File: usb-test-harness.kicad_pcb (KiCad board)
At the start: 4 copper layers, 98 x 85 mm, 85 parts, among them J1 5V_RAW, J10 USB_A_DUAL, J2 GND, J3 V_EXT, J4 USB_A (female down), J5 Conn_01x03_Male, J6 USB_A_DUAL, J7 USB_A_DUAL, J8 USB_A SOFNG USB-05, J9 USB_B_Micro (up), U1 FT24C02A, U2 SE5120ST33, U3 USB2517, U4 APL3511C, U5 APL3511C, U6 APL3511C, U7 APL3511C, U8 APL3511C, U9 APL3511C, Y1 24MHz

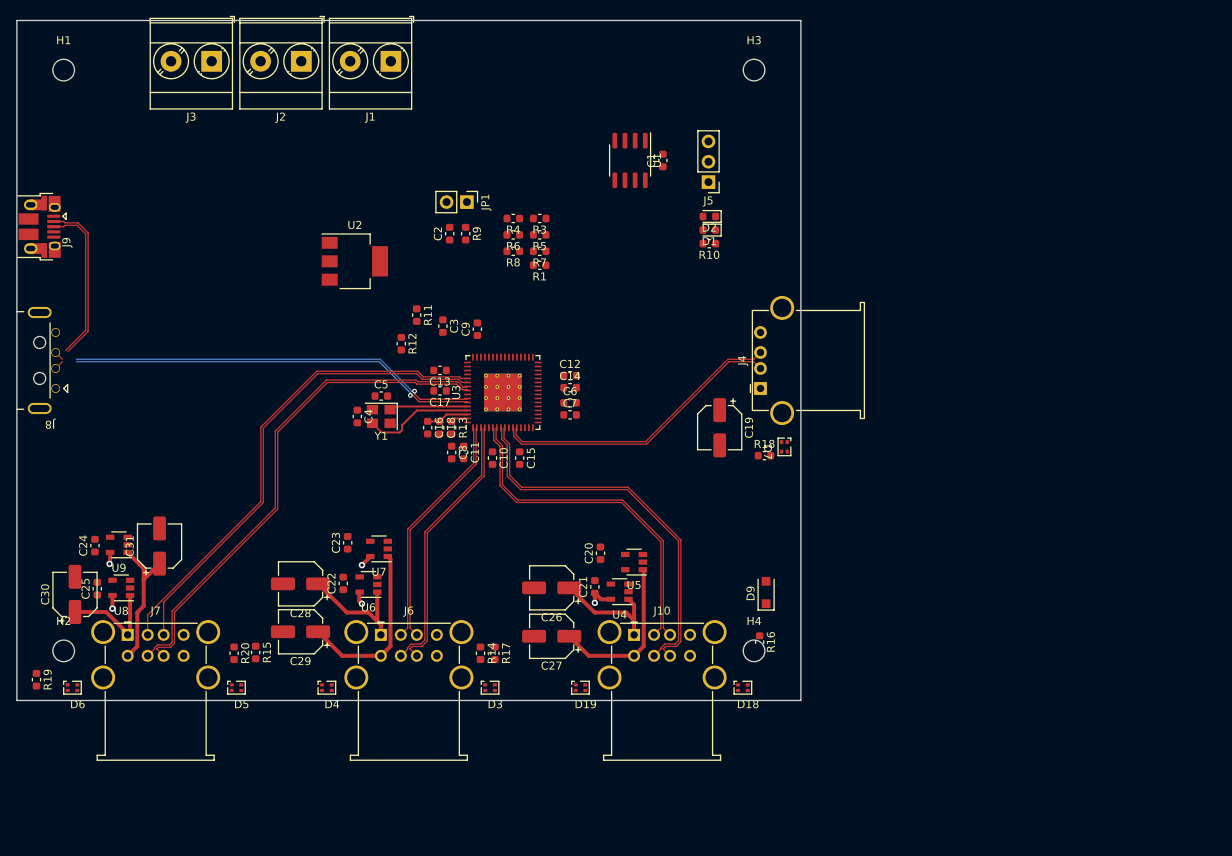
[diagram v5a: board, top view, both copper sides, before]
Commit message: usb-hub: switch to newer amphenol micro b
this makes it feasible to route usb properly.  Then, charge ahead with
routing.  Started with the 3v3 and hub power parts, now continuing with
the enable/overcurrent parts.  leds will be last.
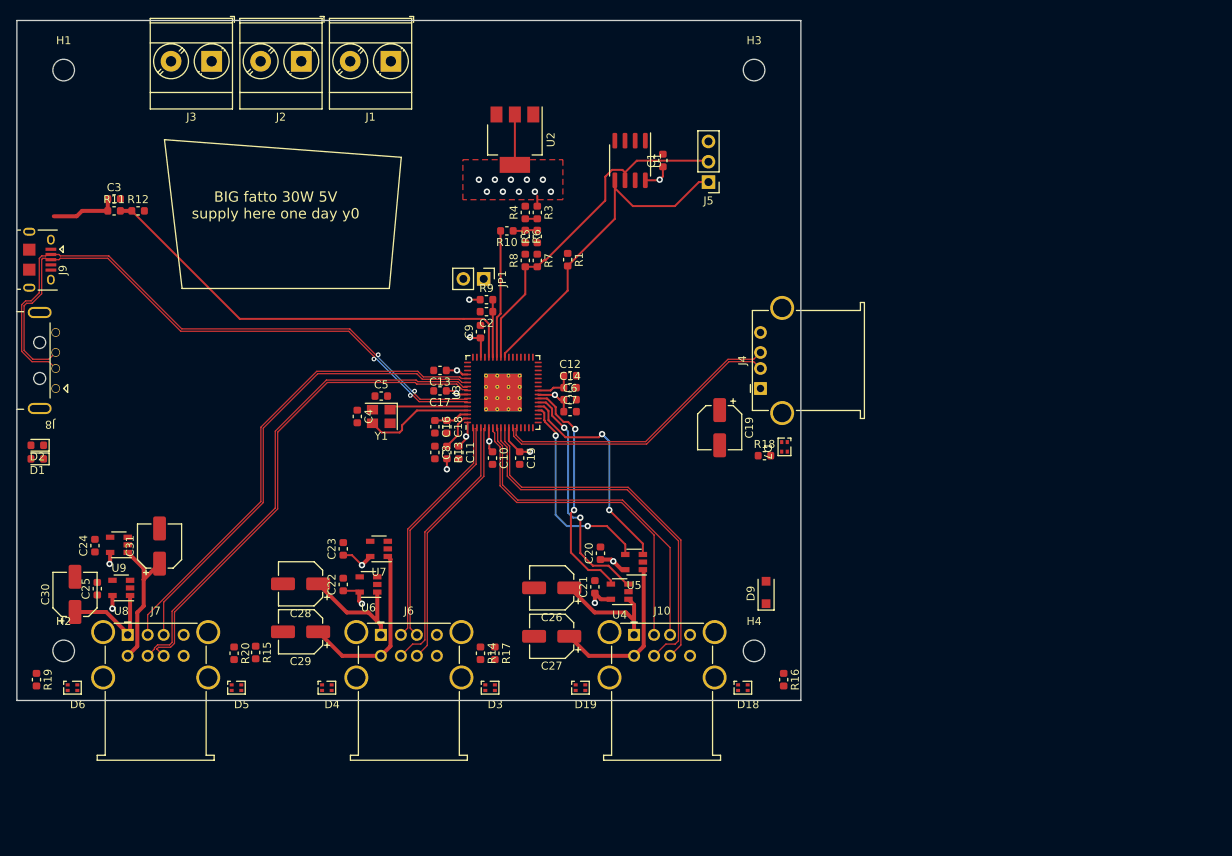
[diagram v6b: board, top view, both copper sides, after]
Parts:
- J9: footprint Connector_USB:USB_Micro-B_Amphenol_10103594-0001LF_Horizontal -> Connector_USB:USB_Micro-B_Amphenol_10118194-0001LF_Horizontal
- moved D1 88.7 mm to (101.8, 105.4)
- moved D2 88.7 mm to (101.8, 103.7)
- moved C3 44.1 mm to (111.4, 72.9), turned to 0 degrees
- moved R11 40.0 mm to (111.4, 74.4), turned to 0 degrees
- moved R12 36.9 mm to (114.4, 74.4), turned to 0 degrees
- moved R10 25.4 mm to (160.5, 76.9)
- moved U2 25.1 mm to (161.5, 65.5), turned to -90 degrees
- moved C2 10.8 mm to (157.9, 87.0), turned to 180 degrees
- moved JP1 9.83 mm to (157.6, 82.9)
- moved R9 8.65 mm to (157.9, 85.5), turned to 0 degrees
- moved R16 5.58 mm to (195.1, 133.0)
- moved J9 4.30 mm to (100.8, 80.5)
- moved R1 3.57 mm to (168.1, 80.5), turned to -90 degrees
- moved R13 3.16 mm to (153.0, 104.6)
- moved C8 2.10 mm to (151.5, 104.6)
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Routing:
- net /upstream-config-leds/VBUS_DET: track 0.00 -> 56.1 mm
- net /upstream-config-leds/CFG_SEL0: track 0.00 -> 44.0 mm
- net /upstream-config-leds/EE_SDA: track 0.00 -> 42.7 mm
- net +3V3: track 0.00 -> 38.5 mm, vias 0 -> 19
- net /downstream-port-power/OC1: track 0.00 -> 29.7 mm, vias 0 -> 2
- net /downstream-port-power/EN1: track 0.00 -> 29.3 mm, vias 0 -> 2
- net /downstream-port-power/OC2: track 0.00 -> 27.6 mm, vias 0 -> 2
- net /downstream-port-power/EN2: track 0.00 -> 25.8 mm, vias 0 -> 2
- net /upstream-config-leds/CFG_SEL1_A: track 0.00 -> 16.0 mm
- net +5V: track 9.62 -> 18.2 mm, vias 5 -> 6
- net /upstream-config-leds/VBUS_UP: track 0.00 -> 8.53 mm
- net /upstream-config-leds/~RESET: track 0.00 -> 7.19 mm
- net /upstream-config-leds/UP-: track 73.1 -> 79.7 mm, vias 1 -> 2
- net /upstream-config-leds/UP+: track 72.5 -> 78.7 mm, vias 1 -> 2
- net /upstream-config-leds/VDD18: track 0.00 -> 4.84 mm
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- added copper zone on F.Cu, net +3V3
- added copper zone on In2.Cu, net +3V3
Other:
- board text added: "BIG fatto 30W 5V supply here one day y0"

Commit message: usb-hub: finish all enable/oc lines, fix warnings
just leds, led drive, usb shields, and the big 5v mainline left.
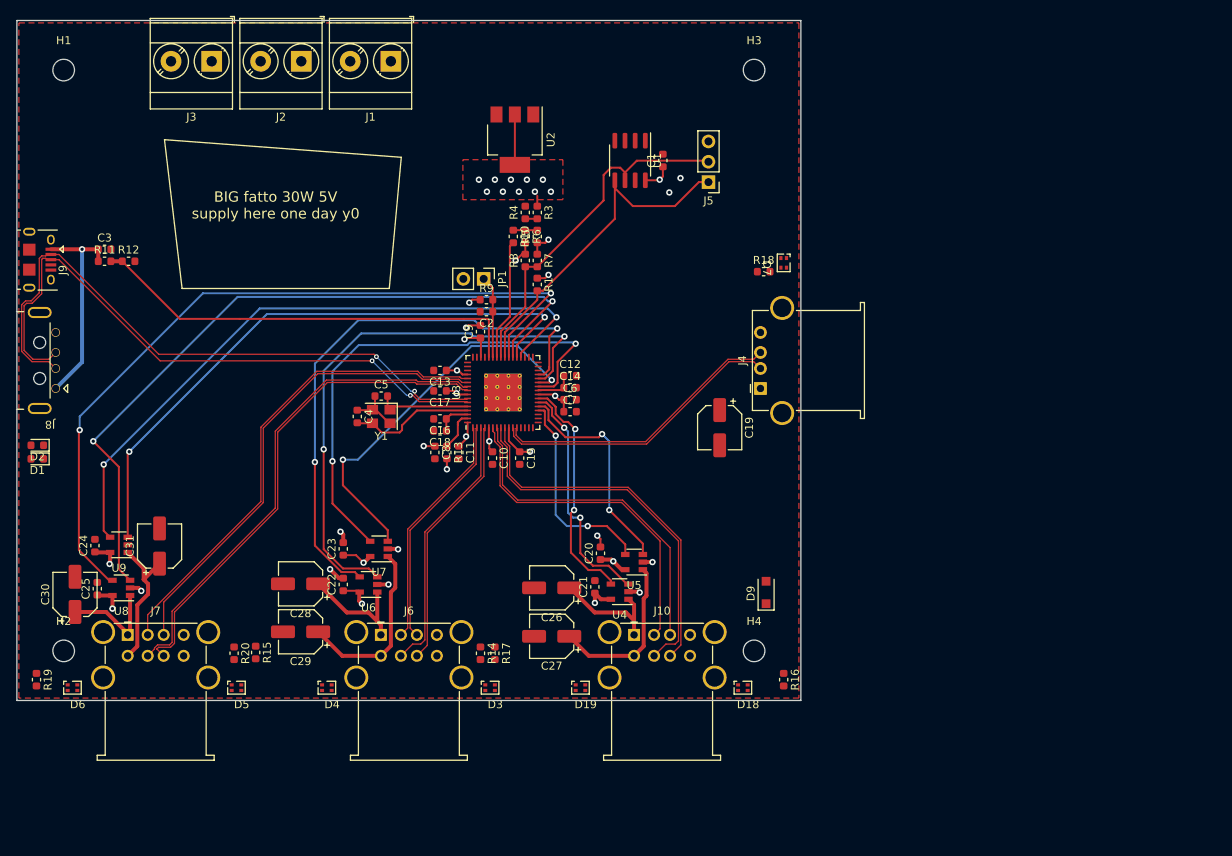
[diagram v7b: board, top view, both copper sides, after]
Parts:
- moved D7 23.0 mm to (195.1, 80.9)
- moved R18 23.0 mm to (192.6, 82.0)
- moved C3 6.41 mm to (110.2, 79.2)
- moved R11 6.41 mm to (110.2, 80.7)
- moved R12 6.41 mm to (113.2, 80.7)
- moved R1 4.90 mm to (164.3, 83.6)
- moved C16 1.18 mm to (152.1, 100.4), turned to 180 degrees
- moved R10 1.06 mm to (161.3, 77.6), turned to -90 degrees
- moved C18 1.00 mm to (152.1, 101.9), turned to 180 degrees
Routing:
- net /downstream-port-power/EN5: track 0.00 -> 97.9 mm, vias 0 -> 2
- net /downstream-port-power/OC5: track 0.00 -> 93.4 mm, vias 0 -> 2
- net /downstream-port-power/EN6: track 0.00 -> 81.4 mm, vias 0 -> 2
- net /downstream-port-power/OC6: track 0.00 -> 76.4 mm, vias 0 -> 2
- net /downstream-port-power/EN3: track 0.00 -> 70.1 mm, vias 0 -> 2
- net /downstream-port-power/OC3: track 0.00 -> 69.7 mm, vias 0 -> 2
- net /downstream-port-power/EN4: track 0.00 -> 63.6 mm, vias 0 -> 2
- net /downstream-port-power/OC4: track 0.00 -> 48.1 mm, vias 0 -> 2
- net GND: track 1.31 -> 24.9 mm, vias 1 -> 13
- net /upstream-config-leds/VBUS_UP: track 8.53 -> 26.2 mm, vias 0 -> 1
- net +3V3: track 38.5 -> 45.3 mm, vias 19 -> 22
- net +5V: track 18.2 -> 21.8 mm
- net /upstream-config-leds/~RESET: track 7.19 -> 10.3 mm
- net /upstream-config-leds/XTAL1: track 13.9 -> 15.8 mm
- net /upstream-config-leds/XTAL2: track 9.85 -> 11.7 mm
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- added copper zone on F.Cu, net GND

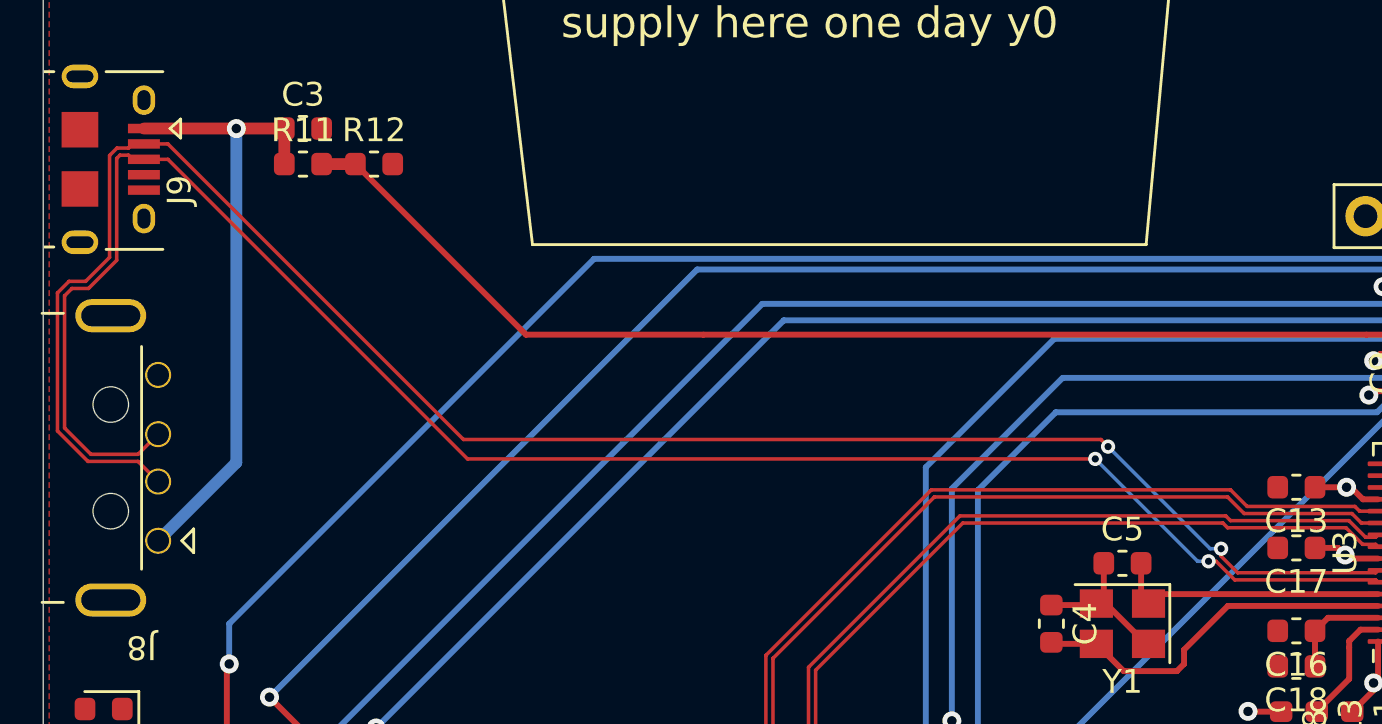
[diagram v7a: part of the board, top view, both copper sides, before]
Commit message: usb-hub: fix broken diff pair after push n shove
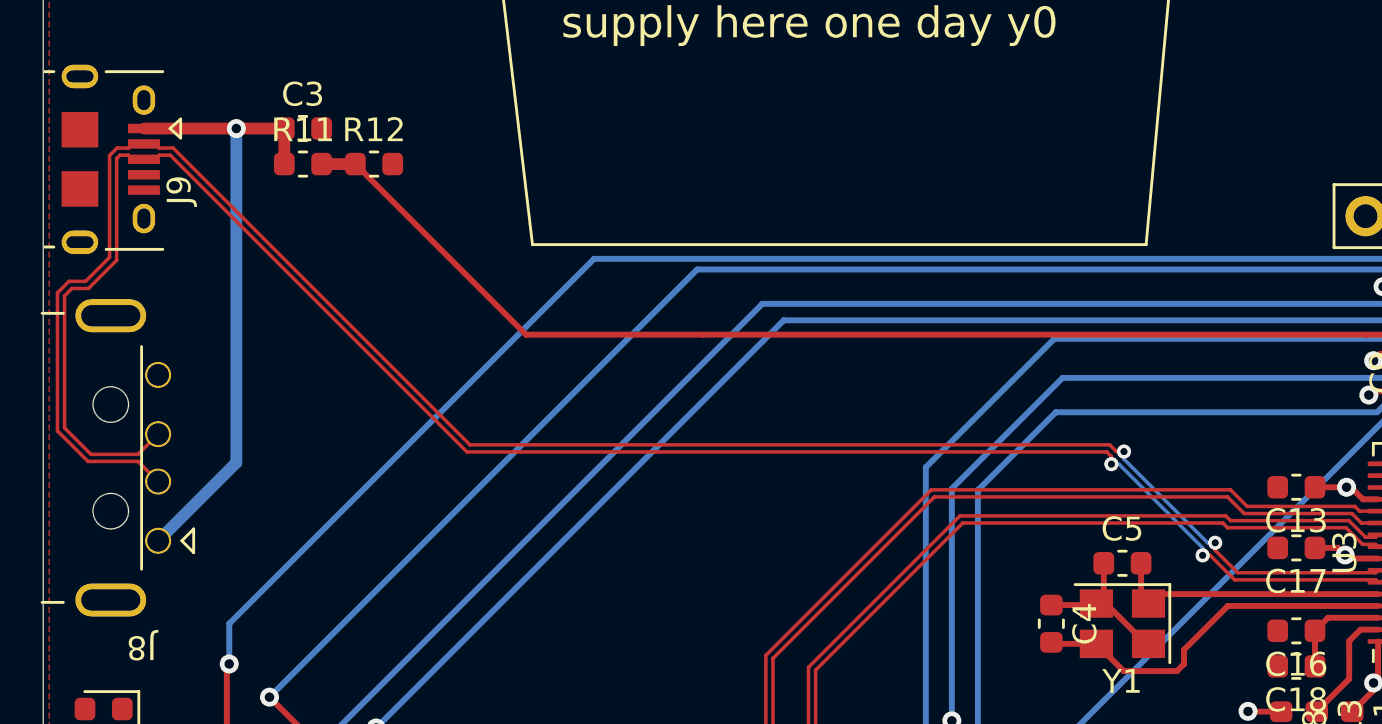
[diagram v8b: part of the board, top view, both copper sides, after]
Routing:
- net /upstream-config-leds/UP+: track 78.2 -> 78.7 mm
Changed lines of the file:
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@@
     (thickness 1.6)
     (drawings 10)
-    (tracks 567)
+    (tracks 576)
     (modules 85)
     (nets 72)
@@
   (gr_line (start 197.25 50.6) (end 99.25 50.6) (layer "Edge.Cuts") (width 0.05))
   (gr_line (start 197.25 135.6) (end 197.25 50.6) (layer "Edge.Cuts") (width 0.05))
+  (segment (start 104.15 80.325) (end 103.975 80.5) (width 0.15) (layer "F.Cu") (net 18))
+  (segment (start 104.612866 80.325) (end 104.15 80.325) (width 0.15) (layer "F.Cu") (net 18))
+  (segment (start 144.334834 93.046967) (end 144.137867 92.85) (width 0.15) (layer "F.Cu") (net 18))
+  (segment (start 117.262134 92.55) (end 104.737134 80.025) (width 0.15) (layer "F.Cu") (net 19))
+  (segment (start 144.865166 92.834834) (end 144.546967 92.834834) (width 0.15) (layer "F.Cu") (net 19))
+  (segment (start 103.975 80.5) (end 103.5 80.5) (width 0.15) (layer "F.Cu") (net 18))
+  (segment (start 117.137866 92.85) (end 104.612866 80.325) (width 0.15) (layer "F.Cu") (net 18))
+  (segment (start 144.262133 92.55) (end 117.262134 92.55) (width 0.15) (layer "F.Cu") (net 19))
+  (segment (start 144.137867 92.85) (end 117.137866 92.85) (width 0.15) (layer "F.Cu") (net 18))
+  (segment (start 144.546967 92.834834) (end 144.262133 92.55) (width 0.15) (layer "F.Cu") (net 19))
+  (segment (start 144.334834 93.365166) (end 144.334834 93.046967) (width 0.15) (layer "F.Cu") (net 18))
+  (segment (start 103.975 79.85) (end 103.5 79.85) (width 0.15) (layer "F.Cu") (net 19))
+  (segment (start 104.737134 80.025) (end 104.15 80.025) (width 0.15) (layer "F.Cu") (net 19))
+  (segment (start 104.15 80.025) (end 103.975 79.85) (width 0.15) (layer "F.Cu") (net 19))
+  (segment (start 144.653033 93.365166) (end 144.334834 93.365166) (width 0.15) (layer "B.Cu") (net 18))
+  (via (at 144.334834 93.365166) (size 0.6) (drill 0.3) (layers "F.Cu" "B.Cu") (net 18))
+  (segment (start 144.865166 93.153033) (end 144.865166 92.834834) (width 0.15) (layer "B.Cu") (net 19))
+  (segment (start 148.184834 97.215166) (end 148.184834 96.896967) (width 0.15) (layer "B.Cu") (net 18))
+  (segment (start 148.184834 96.896967) (end 144.653033 93.365166) (width 0.15) (layer "B.Cu") (net 18))
+  (via (at 144.865166 92.834834) (size 0.6) (drill 0.3) (layers "F.Cu" "B.Cu") (net 19))
+  (segment (start 148.715166 96.684834) (end 148.396967 96.684834) (width 0.15) (layer "B.Cu") (net 19))
+  (segment (start 148.396967 96.684834) (end 144.865166 93.153033) (width 0.15) (layer "B.Cu") (net 19))
+  (via (at 148.715166 96.684834) (size 0.6) (drill 0.3) (layers "F.Cu" "B.Cu") (net 19))
+  (segment (start 155.4875 97.95) (end 149.662133 97.95) (width 0.15) (layer "F.Cu") (net 19))
+  (segment (start 149.662133 97.95) (end 148.715166 97.003033) (width 0.15) (layer "F.Cu") (net 19))
+  (via (at 148.184834 97.215166) (size 0.6) (drill 0.3) (layers "F.Cu" "B.Cu") (net 18))
+  (segment (start 155.5875 98.35) (end 155.4875 98.25) (width 0.15) (layer "F.Cu") (net 18))
+  (segment (start 155.5875 97.85) (end 155.4875 97.95) (width 0.15) (layer "F.Cu") (net 19))
+  (segment (start 155.4875 98.25) (end 149.537867 98.25) (width 0.15) (layer "F.Cu") (net 18))
+  (segment (start 149.537867 98.25) (end 148.503033 97.215166) (width 0.15) (layer "F.Cu") (net 18))
+  (segment (start 148.503033 97.215166) (end 148.184834 97.215166) (width 0.15) (layer "F.Cu") (net 18))
+  (segment (start 148.715166 97.003033) (end 148.715166 96.684834) (width 0.15) (layer "F.Cu") (net 19))
   (segment (start 158.3 104.1125) (end 158.7 104.5125) (width 0.25) (layer "F.Cu") (net 6) (status 8000))
   (segment (start 158.25 103.15) (end 158.3 103.2) (width 0.25) (layer "F.Cu") (net 6) (status 8000))
@@
   (via (at 166.7 87.7) (size 0.8) (drill 0.4) (layers "F.Cu" "B.Cu") (net 26))
   (segment (start 145.6156 114.3156) (end 145.6156 115.7) (width 0.25) (layer "F.Cu") (net 36))
-  (segment (start 147.973407 97.465166) (end 143.653258 93.145017) (width 0.15) (layer "B.Cu") (net 18))
   (via (at 140 105.5) (size 0.8) (drill 0.4) (layers "F.Cu" "B.Cu") (net 36))
-  (segment (start 148.965166 96.934834) (end 148.503554 96.934834) (width 0.15) (layer "B.Cu") (net 19))
-  (segment (start 103.5 80.5) (end 104.512501 80.5) (width 0.15) (layer "F.Cu") (net 18))
-  (via (at 144.19373 92.62501) (size 0.6) (drill 0.3) (layers "F.Cu" "B.Cu") (net 19))
-  (segment (start 117.157518 93.145017) (end 143.653258 93.145017) (width 0.15) (layer "F.Cu") (net 18))
   (segment (start 138.7 110.9844) (end 138.7 105.7) (width 0.25) (layer "F.Cu") (net 37) (status 8000))
-  (via (at 143.653258 93.145017) (size 0.6) (drill 0.3) (layers "F.Cu" "B.Cu") (net 18))
   (segment (start 140 105.5) (end 140 108.7) (width 0.25) (layer "F.Cu") (net 36))
-  (segment (start 148.434834 97.465166) (end 147.973407 97.465166) (width 0.15) (layer "B.Cu") (net 18))
-  (segment (start 103.5 79.85) (end 104.512501 79.85) (width 0.15) (layer "F.Cu") (net 19))
-  (segment (start 104.512501 79.85) (end 116.987512 92.325011) (width 0.15) (layer "F.Cu") (net 19))
-  (segment (start 143.893731 92.325011) (end 144.19373 92.62501) (width 0.15) (layer "F.Cu") (net 19))
   (segment (start 143.4156 115.7) (end 138.7 110.9844) (width 0.25) (layer "F.Cu") (net 37) (status 8000))
-  (segment (start 148.503554 96.934834) (end 144.19373 92.62501) (width 0.15) (layer "B.Cu") (net 19))
-  (segment (start 104.512501 80.5) (end 117.157518 93.145017) (width 0.15) (layer "F.Cu") (net 18))
-  (segment (start 116.987512 92.325011) (end 143.893731 92.325011) (width 0.15) (layer "F.Cu") (net 19))
   (segment (start 140 108.7) (end 145.6156 114.3156) (width 0.25) (layer "F.Cu") (net 36))
   (via (at 138.7 105.7) (size 0.8) (drill 0.4) (layers "F.Cu" "B.Cu") (net 37))
@@
   (segment (start 160.75 101.5125) (end 160.75 103.1625) (width 0.25) (layer "F.Cu") (net 6))
   (segment (start 160.75 103.1625) (end 162.1 104.5125) (width 0.25) (layer "F.Cu") (net 6))
-  (via (at 148.434834 97.465166) (size 0.6) (drill 0.3) (layers "F.Cu" "B.Cu") (net 18))
-  (via (at 148.965166 96.934834) (size 0.6) (drill 0.3) (layers "F.Cu" "B.Cu") (net 19))
-  (segment (start 149.537867 98.25) (end 148.753033 97.465166) (width 0.15) (layer "F.Cu") (net 18))
-  (segment (start 155.5875 98.35) (end 155.4875 98.25) (width 0.15) (layer "F.Cu") (net 18))
-  (segment (start 155.4875 97.95) (end 149.662133 97.95) (width 0.15) (layer "F.Cu") (net 19))
-  (segment (start 155.4875 98.25) (end 149.537867 98.25) (width 0.15) (layer "F.Cu") (net 18))
-  (segment (start 148.753033 97.465166) (end 148.434834 97.465166) (width 0.15) (layer "F.Cu") (net 18))
-  (segment (start 148.965166 97.253033) (end 148.965166 96.934834) (width 0.15) (layer "F.Cu") (net 19))
-  (segment (start 155.5875 97.85) (end 155.4875 97.95) (width 0.15) (layer "F.Cu") (net 19))
-  (segment (start 149.662133 97.95) (end 148.965166 97.253033) (width 0.15) (layer "F.Cu") (net 19))
   (segment (start 149.237866 96.05) (end 149.037866 95.85) (width 0.15) (layer "F.Cu") (net 16))
   (segment (start 154.362134 95.75) (end 149.362134 95.75) (width 0.15) (layer "F.Cu") (net 15))
